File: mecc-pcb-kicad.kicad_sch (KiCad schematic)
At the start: 51 parts, among them J1 UI BUS, J2 VBatt -> 5V, J3 Wave_Gauge, J4 5V -> 3.3V, J5 PDQE15-Q48-D24-D, J6 VESC IN, J7 IV Sens, Q1 NMOS, Q2 NMOS, Q3 PMOS, Q4 PMOS, U1 SEN-16407

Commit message: merged with Nathan's branch
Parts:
- removed J7: IV Sens, Connector_Molex:Molex_KK-254_AE-6410-03A_1x03_P2.54mm_Vertical, symbol Connector:Conn_01x03_Socket
- added J8: Torq_SENS, Connector_Molex:Molex_KK-254_AE-6410-04A_1x04_P2.54mm_Vertical, symbol Connector:Conn_01x04_Socket
- added SW1: Reset, Button_Switch_SMD:SW_SPST_SKQG_WithoutStem, symbol Switch:SW_Push
- added U2: SN74HCS09QPWRQ1, SN74HCS09QPWRQ1:SO14_PW_TEX, symbol SN74HCS09QPWRQ1:SN74HCS09QPWRQ1
- added U3: SN74LVC1G139DCUR, SN74LVC1G139DCUR:DCU0008A_N, symbol SN74LVC1G139DCUR:SN74LVC1G139DCUR
- J1: footprint Connector_Molex:Molex_KK-254_AE-6410-08A_1x08_P2.54mm_Vertical -> Connector_Molex:Molex_KK-254_AE-6410-07A_1x07_P2.54mm_Vertical; symbol Connector:Conn_01x09_Socket -> Connector:Conn_01x07_Socket
- R7, R8: value 4.7k -> 10k
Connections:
- net +24V: now also J8.4 (Pin_4)
- net +3.3V: now also SW1.1, U2.14 (VCC), U3.8 (VCC)
- net ADVANCE_BUTTON_RED: now also J1.4 (Pin_4); no longer J1.6 (Pin_6)
- net GND: now also J8.1 (Pin_1), J8.3 (Pin_3), U2.7 (GND), U3.4 (GND)
- net HIGH_IN: now also U2.2 (1B); no longer J1.4 (Pin_4)
- net HIGH_SIDE_STM: now also U2.3 (1Y); no longer J1.7 (Pin_7)
- net IO_ESTOP: now also U2.1 (1A), U2.4 (2A)
- net LOW_OUT: no longer J1.5 (Pin_5)
- net PRE_LOW_DIS_STM: now also U2.6 (2Y); no longer J1.8 (Pin_8)
- net RESET: now also J1.5 (Pin_5), SW1.2; no longer J1.9 (Pin_9)
- net TORQUE_SENSOR: now also J8.2 (Pin_2)
- new net LOW_IN: U2.5 (2B)
- new net TORQ_SWITCH_1: J1.6 (Pin_6), U3.1 (A)
- new net TORQ_SWITCH_2: J1.7 (Pin_7), U3.2 (B)

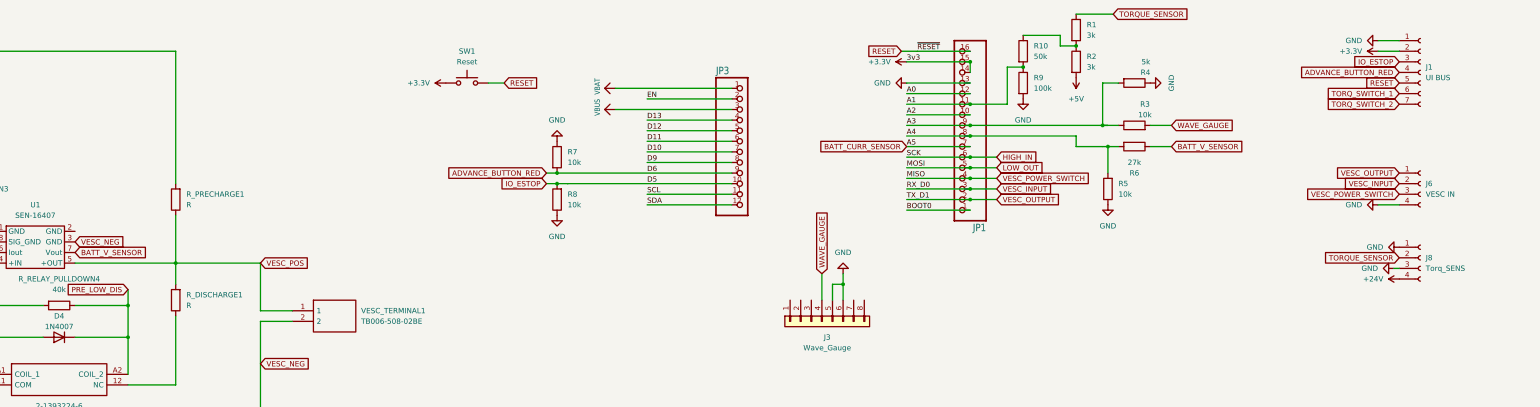
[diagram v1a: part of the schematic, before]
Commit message: Implemented all of list except for CMOS stuff
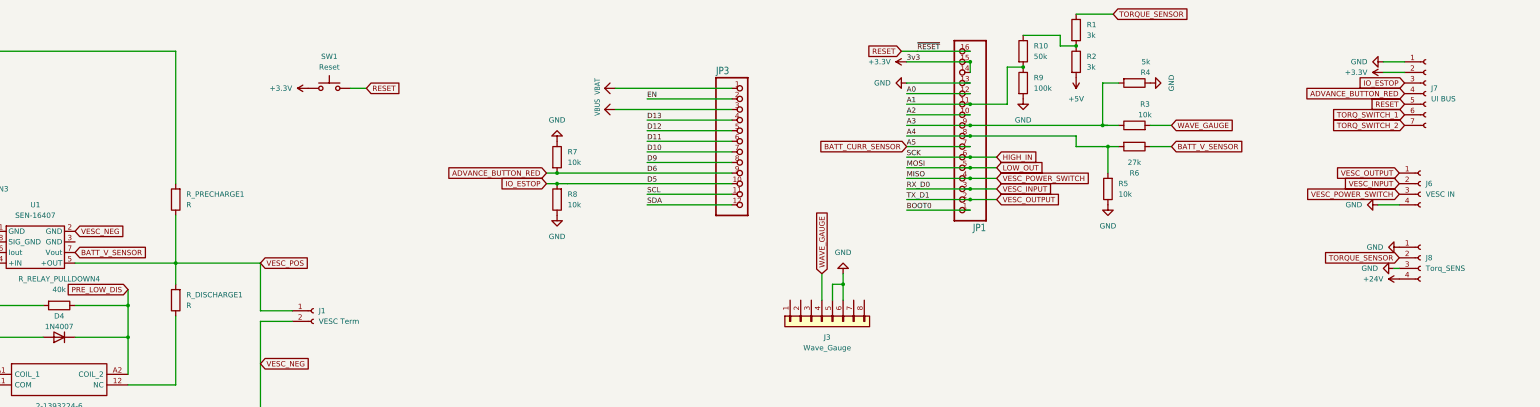
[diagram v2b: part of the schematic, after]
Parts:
- removed J1: UI BUS, Connector_Molex:Molex_KK-254_AE-6410-07A_1x07_P2.54mm_Vertical, symbol Connector:Conn_01x07_Socket
- removed VESC_TERMINAL1: TB006-508-02BE, MECC-CUI-Screw-terminal:TB00650802BE, symbol MECC-CUI-Screw-terminal:TB006-508-02BE
- added J1: VESC Term, Connector:Banana_Jack_2Pin, symbol Connector:Conn_01x02_Socket
- added J7: UI BUS, Connector_Molex:Molex_KK-254_AE-6410-07A_1x07_P2.54mm_Vertical, symbol Connector:Conn_01x07_Socket
- J4: footprint Package_SIP:SIP-8_19x3mm_P2.54mm -> Connector_PinHeader_2.54mm:PinHeader_1x04_P2.54mm_Vertical
- Q1, Q2: footprint Package_TO_SOT_THT:TO-92_Inline -> Library:WEC_NMOS
- Q3, Q4: footprint Package_TO_SOT_THT:TO-220-3_Vertical -> Library:WEC_PMOS
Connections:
- net +3.3V: now also J7.2 (Pin_2)
- net ADVANCE_BUTTON_RED: now also J7.4 (Pin_4)
- net GND: now also J7.1 (Pin_1)
- net IO_ESTOP: now also J7.3 (Pin_3)
- net RESET: now also J7.5 (Pin_5)
- net TORQ_SWITCH_1: now also J7.6 (Pin_6)
- net TORQ_SWITCH_2: now also J7.7 (Pin_7)
- net VESC_NEG: now also U1.2 (GND), J1.2 (Pin_2); no longer U1.3 (GND)
- net VESC_POS: now also J1.1 (Pin_1)

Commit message: Implemented some of becca's changes
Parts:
- J7: footprint Connector_Molex:Molex_KK-254_AE-6410-07A_1x07_P2.54mm_Vertical -> Connector_Molex:Molex_KK-254_AE-6410-08A_1x08_P2.54mm_Vertical; symbol Connector:Conn_01x07_Socket -> Connector:Conn_01x08_Socket
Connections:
- net D10 is gone; now on net Torq_SW_Mode_3: JP3.7
- net D11 is gone; now on net Torq_SW_Mode_2: JP3.6
- net D12 is gone; now on net Torq_SW_Mode_1: JP3.5
- net LOW_OUT is gone; now on net LOW_IN: JP1.5
- net Torq_SW_Mode_3: now reaches U3.5 (Y2)
- net Torq_SW_Mode_2: now reaches U3.6 (Y1)
- net Torq_SW_Mode_1: now reaches U3.7 (Y0)
- net D9 renamed Ref_Model_SW
- net Ref_Model_SW: now also J7.8 (Pin_8)
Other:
- moved on the sheet: R7, R8

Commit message: I don't even think I made changes I'm just paranoid
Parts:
- added Q5: NMOS, Library:WEC_NMOS, symbol Transistor_FET:2N7000
- added R11, R12: 10k, Resistor_THT:R_Axial_DIN0204_L3.6mm_D1.6mm_P7.62mm_Horizontal, symbol Device:R
- J7: symbol Connector:Conn_01x08_Socket -> Connector:Conn_01x09_Socket
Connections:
- net +5V: now also Q5.3 (D)
- net BATT_NEG: now also C1.2, J5.2 (GND); no longer C1.1, J5.3 (VIN)
- net BATT_POS: now also C1.1, J5.3 (VIN); no longer C1.2, J5.2 (GND)
- net GND: now also R11.2, R12.2
- net DCDC_SW: now reaches J2.3 (Pin_3)
- net DCDC_SW: now also J7.9 (Pin_9), Q5.2 (G), R11.1
- net at J5.1 (CTRL): now also Q5.1 (S), R12.1
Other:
- moved on the sheet: C1, J4, J6, J8

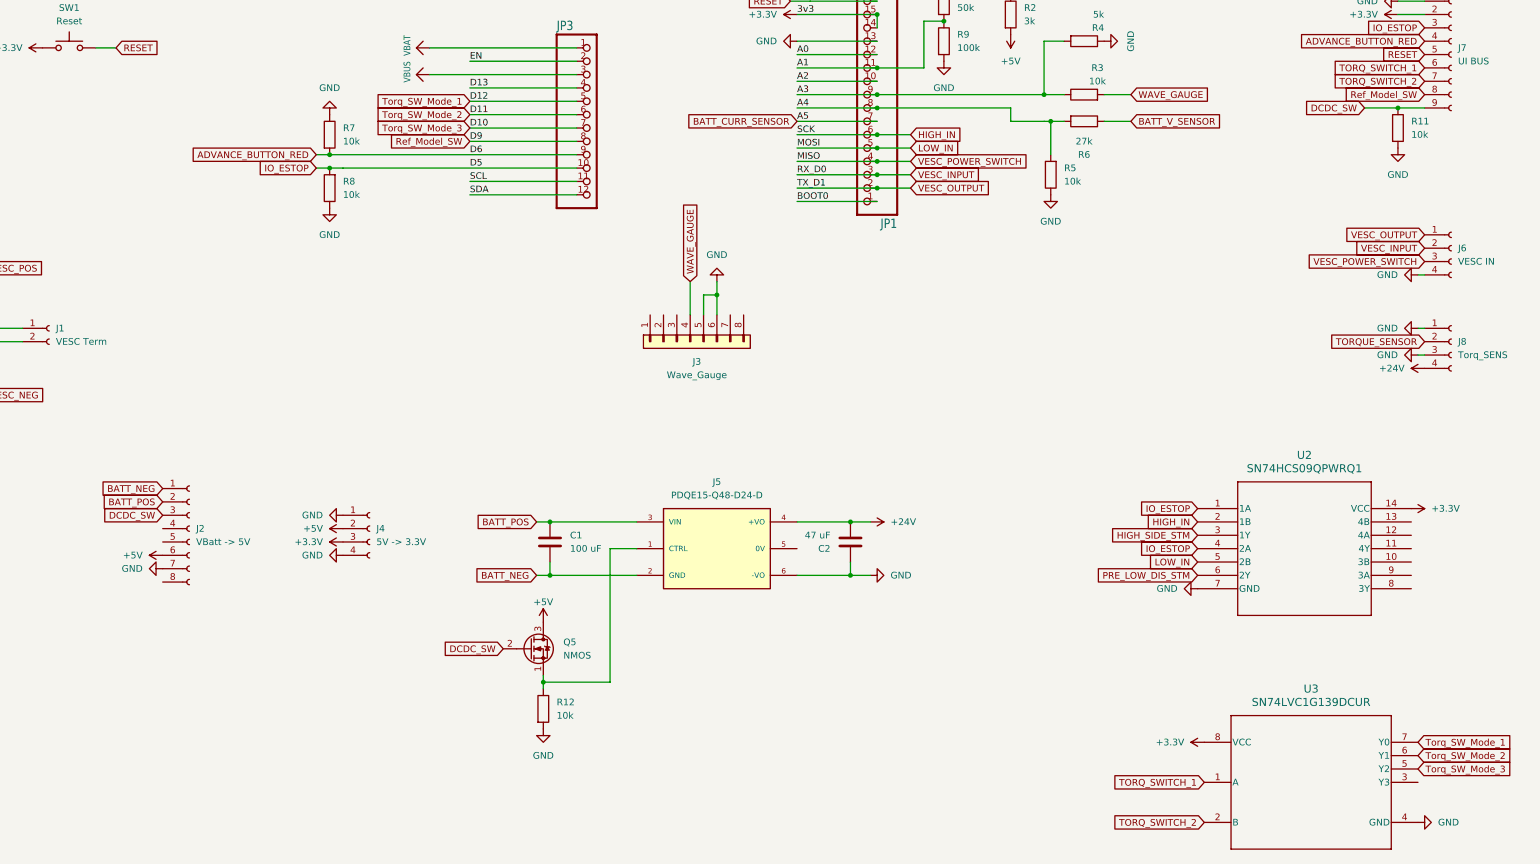
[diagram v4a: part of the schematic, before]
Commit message: Added a PGND and AGND connection, and cleaned up some routing.
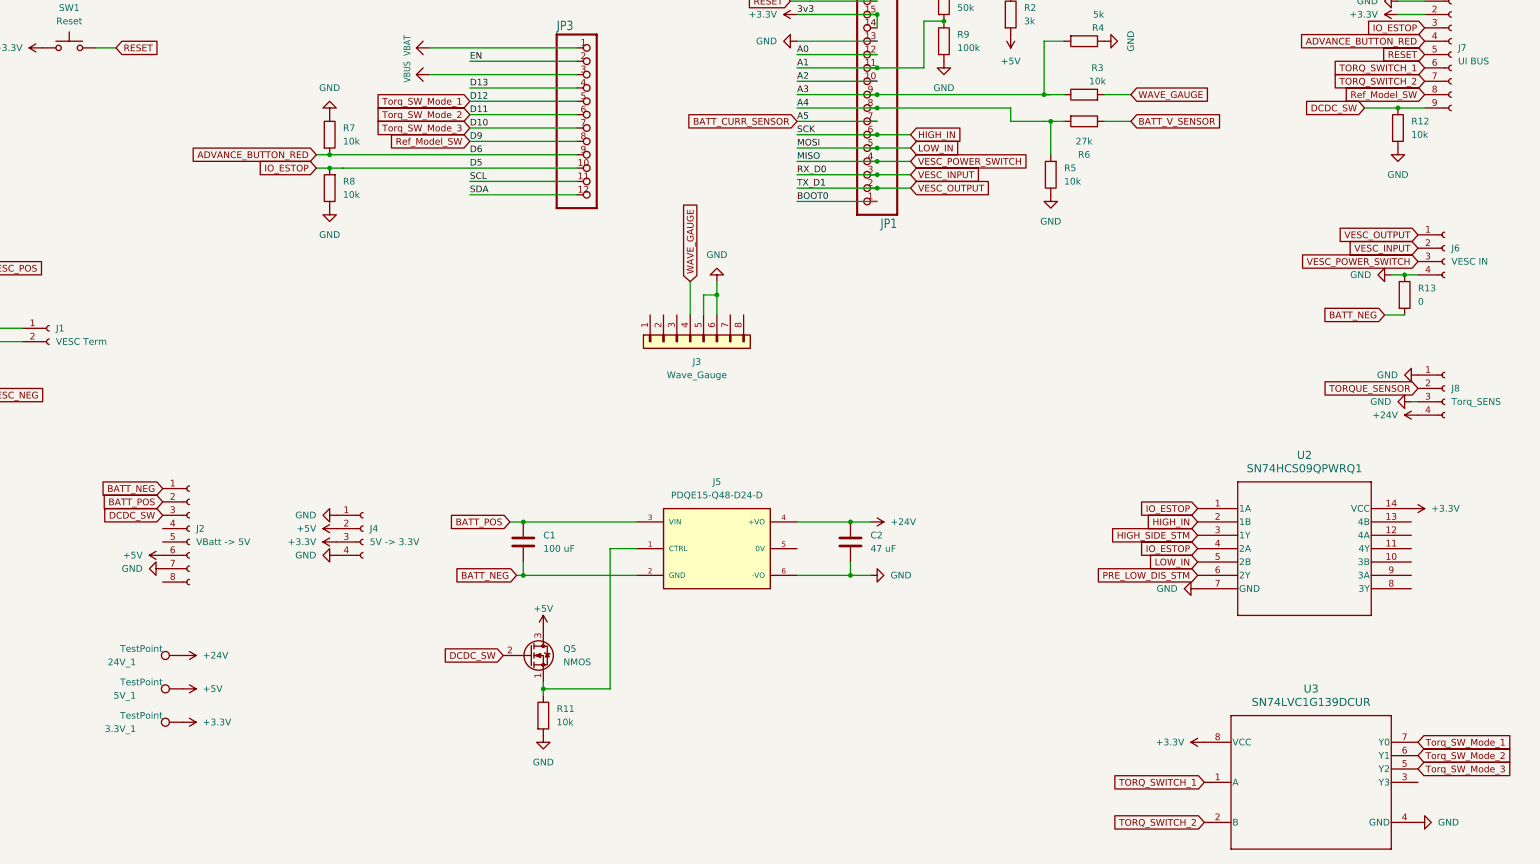
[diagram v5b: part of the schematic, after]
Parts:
- added 24V_1, 3.3V_1, 5V_1: TestPoint, TestPoint:TestPoint_THTPad_4.0x4.0mm_Drill2.0mm, symbol Connector:TestPoint
- added R13: 0, Resistor_THT:R_Axial_DIN0204_L3.6mm_D1.6mm_P7.62mm_Horizontal, symbol Device:R
- J7: footprint Connector_Molex:Molex_KK-254_AE-6410-08A_1x08_P2.54mm_Vertical -> Connector_Molex:Molex_KK-254_AE-6410-09A_1x09_P2.54mm_Vertical
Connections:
- net +24V: now also C2.1, 24V_1.1; no longer C2.2
- net +3.3V: now also 3.3V_1.1
- net +5V: now also 5V_1.1
- net BATT_NEG: now also R13.2
- net DCDC_SW: now also R12.1; no longer R11.1
- net GND: now also C2.2, R13.1; no longer C2.1
- net at J5.1 (CTRL), Q5.1 (S): now also R11.1; no longer R12.1
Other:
- moved on the sheet: J4, J6, J8

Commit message: Implemented Becca's comments. Board should be ready for final review
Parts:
- added J9: IV_Sens, Connector_Molex:Molex_KK-254_AE-6410-03A_1x03_P2.54mm_Vertical, symbol Connector:Conn_01x03_Socket
- J6: footprint Connector_Molex:Molex_KK-254_AE-6410-04A_1x04_P2.54mm_Vertical -> Connector_Molex:Molex_KK-254_AE-6410-05A_1x05_P2.54mm_Vertical
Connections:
- net BATT_CURR_SENSOR: now also J9.2 (Pin_2)
- net BATT_NEG: no longer C1.2, J2.1 (Pin_1), J5.2 (GND), R13.2
- net BATT_V_SENSOR: now also J9.3 (Pin_3)
- net GND: now also J9.1 (Pin_1)
- net VESC_NEG: now also C1.2, J2.1 (Pin_1), J5.2 (GND), R13.2
- net HIGH_SIDE_STM renamed HIGH_SIDE_ANDOUT
- net PRE_LOW_DIS renamed PRE_DIS
- net PRE_LOW_DIS_STM renamed PRE_DIS_ANDOUT
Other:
- moved on the sheet: U2, U3

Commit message: Added Gerber files
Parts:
- added GND_1, TP10, TP11, TP12, TP13, TP14, TP15, TP16, TP17, TP18, TP7, TP9: TestPoint, TestPoint:TestPoint_THTPad_4.0x4.0mm_Drill2.0mm, symbol Connector:TestPoint
- added SW2: Reset, Button_Switch_SMD:SW_SPST_SKQG_WithoutStem, symbol Switch:SW_Push
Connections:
- net +3.3V: now also SW2.1
- net A1: now also TP10.1
- net A3: now also TP11.1
- net A4: now also TP12.1
- net ADVANCE_BUTTON_RED: now also TP9.1
- net BATT_POS: now also TP14.1
- net BOOT0: now also SW2.2
- net DCDC_SW: now also TP17.1
- net GND: now also GND_1.1, TP13.1
- net IO_ESTOP: now also TP16.1
- net PRE_DIS: now also TP7.1
- net VESC_NEG: now also TP15.1
- net at J5.1 (CTRL), Q5.1 (S), R11.1: now also TP18.1
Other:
- moved on the sheet: R10, R4, R5, R6, R7, R8, R9

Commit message: changed pulldown resistor values to match the resistors we have in the lab (5.1k)
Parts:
- R11, R12, R7, R8, RHIGH_10k1, RHIGH_10k2: value 10k -> 5.1k
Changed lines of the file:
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@@
       (effects (font (size 1.27 1.27)) (justify left))
     )
-    (property "Value" "10k" (at 298.45 49.53 0)
+    (property "Value" "5.1k" (at 298.45 49.53 0)
       (effects (font (size 1.27 1.27)) (justify left))
     )
@@
       (effects (font (size 1.27 1.27)))
     )
-    (property "Value" "10k" (at 62.23 147.32 90)
+    (property "Value" "5.1k" (at 62.23 147.32 90)
       (effects (font (size 1.27 1.27)))
     )
@@
       (effects (font (size 1.27 1.27)) (justify right))
     )
-    (property "Value" "10k" (at 298.45 59.69 0)
+    (property "Value" "5.1k" (at 298.45 59.69 0)
       (effects (font (size 1.27 1.27)) (justify right))
     )
@@
       (effects (font (size 1.27 1.27)) (justify left))
     )
-    (property "Value" "10k" (at 350.52 160.02 0)
+    (property "Value" "5.1k" (at 350.52 160.02 0)
       (effects (font (size 1.27 1.27)) (justify left))
     )
@@
       (effects (font (size 1.27 1.27)))
     )
-    (property "Value" "10k" (at 62.23 181.61 90)
+    (property "Value" "5.1k" (at 62.23 181.61 90)
       (effects (font (size 1.27 1.27)))
     )
@@
       (effects (font (size 1.27 1.27)) (justify left))
     )
-    (property "Value" "10k" (at 513.08 48.26 0)
-      (effects (font (size 1.27 1.27)) (justify left))
-    )
+    (property "Value" "5.1k" (at 513.08 48.26 0)
+      (effects (font (size 1.27 1.27)) (justify left))
+    )
